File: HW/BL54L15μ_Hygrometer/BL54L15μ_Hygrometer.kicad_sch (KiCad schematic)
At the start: 36 parts, among them IC1 nrf54L 453-00223R, J1 Conn_Qwiic, J2 Conn_ARM_JTAG_SWD_10, SW1 Reset, U1 nPM2100-QEXX, U2 SHT4x, U3 STCC4-D-R3, U5 BME688, X1 32.768 kHz

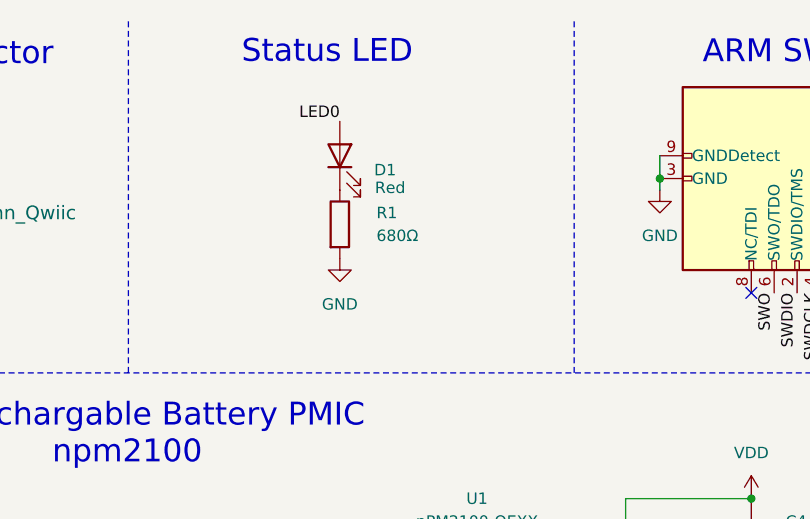
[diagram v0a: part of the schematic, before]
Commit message: Cleanup Hygrometer BOM
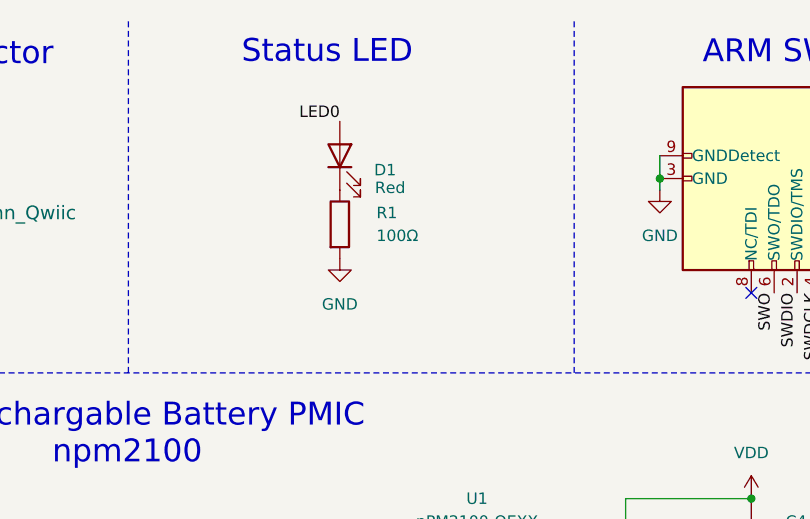
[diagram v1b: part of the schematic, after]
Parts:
- R1: value 680Ω -> 100Ω; Part Number RC0603JR-13680RL -> RC0603FR-07100RL
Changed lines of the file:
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@@
 			)
 		)
-		(property "Value" "680Ω"
+		(property "Value" "100Ω"
 			(at 87.884 36.83 0)
 			(effects
@@
 			)
 		)
-		(property "Part Number" "RC0603JR-13680RL"
+		(property "Part Number" "RC0603FR-07100RL"
 			(at 83.82 35.56 0)
 			(effects

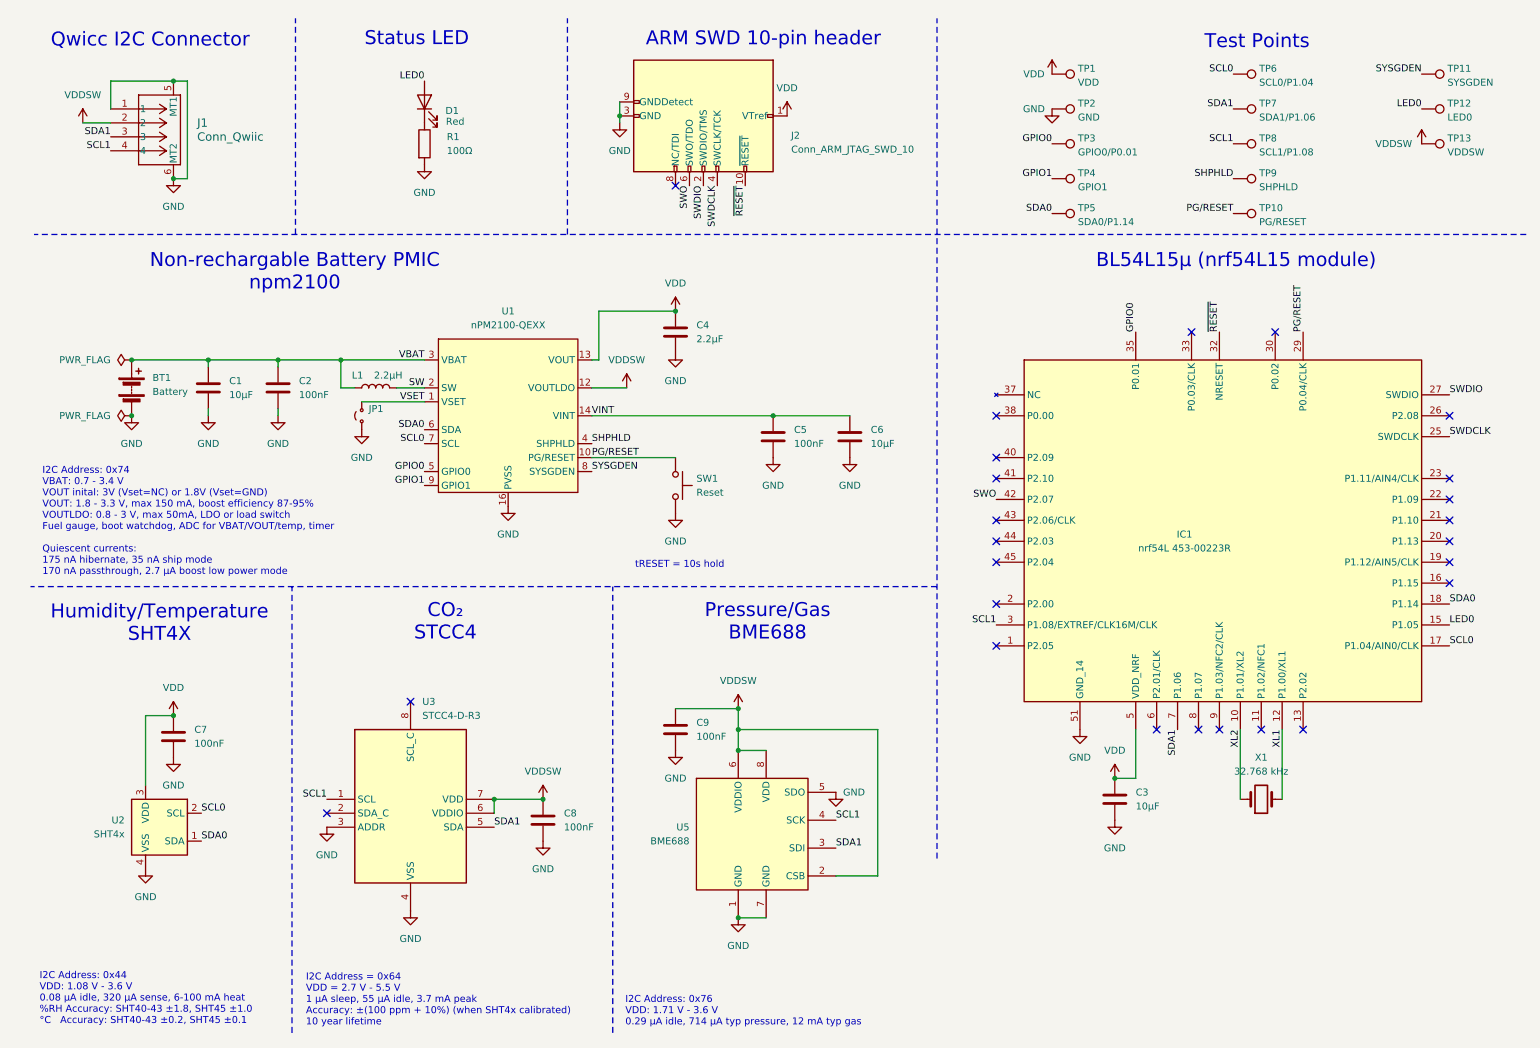
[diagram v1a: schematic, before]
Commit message: BL54L15μ Hygrometer 2026v4 with leak sensing
- Switch to CR2 battery
- Drop power-hungry STCC4/BME688 sensors
- Circular design with M1.2 mounting holes
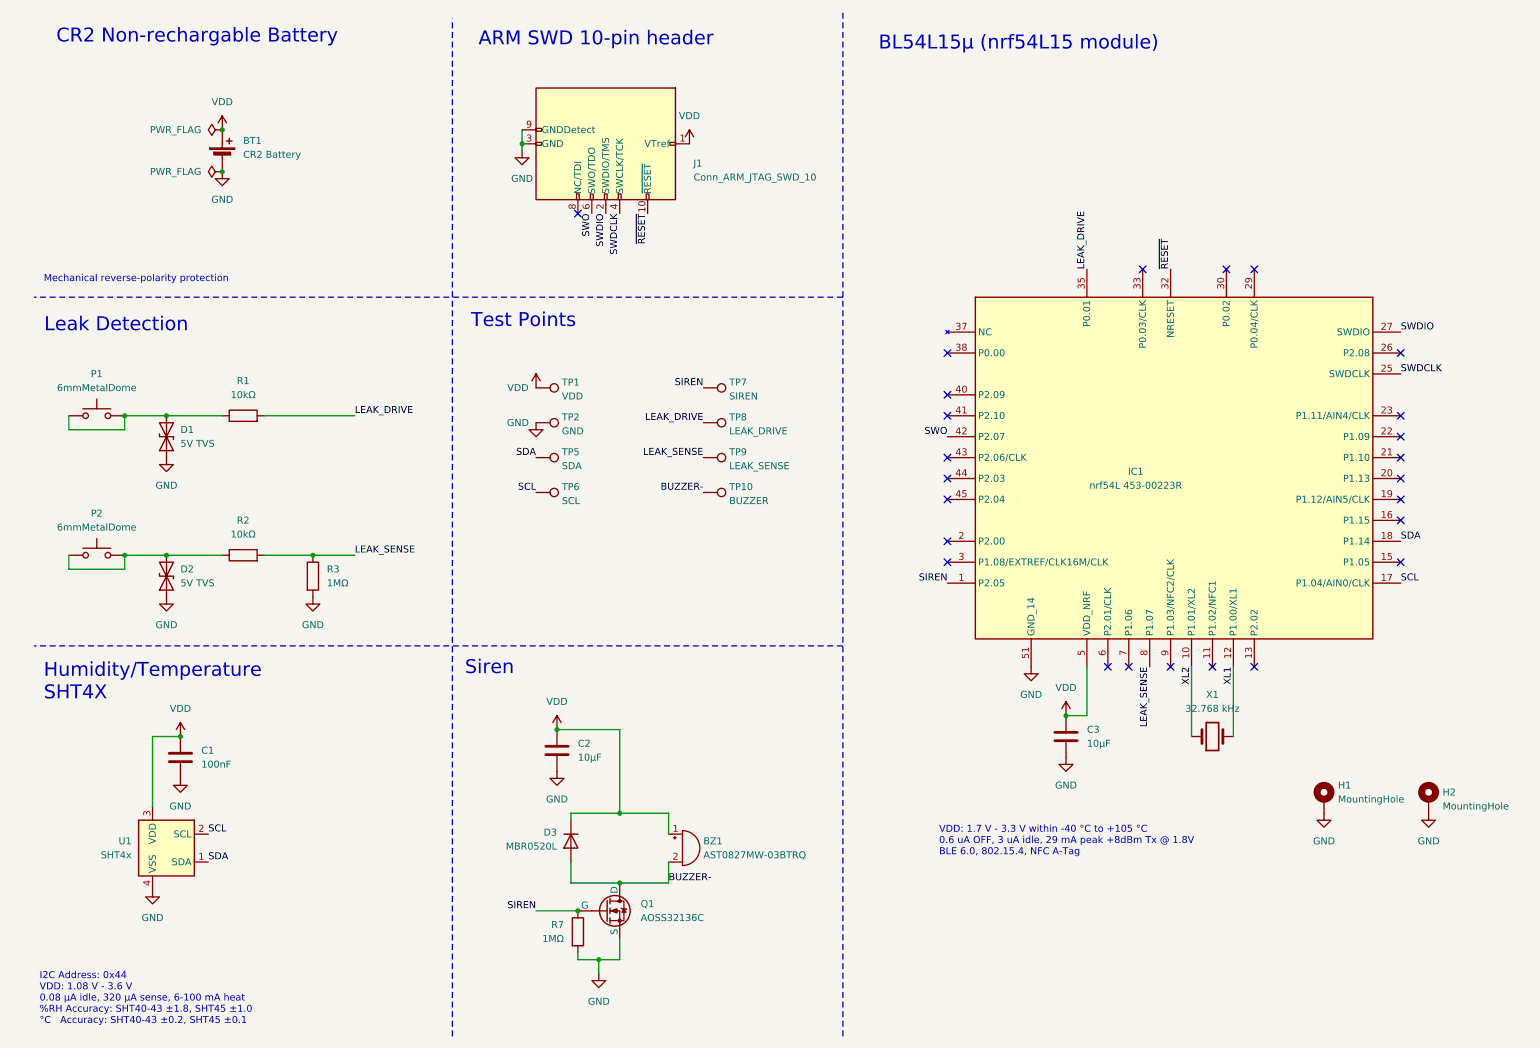
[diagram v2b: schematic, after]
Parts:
- removed C1, C6: 10μF, Capacitor_SMD:C_0603_1608Metric, symbol Device:C
- removed C4: 2.2μF, Capacitor_SMD:C_0402_1005Metric, symbol Device:C
- removed C5, C8, C9: 100nF, Capacitor_SMD:C_0402_1005Metric, symbol Device:C
- removed D1: PWRLED, LED_SMD:LED_0603_1608Metric, symbol Device:LED
- removed J1: Conn_Qwiic, SM04B_SRSS_TB:CONN_SM04B-SRSS-TB_JST, symbol SM04B_SRSS_TB:SM04B-SRSS-TB
- removed JP1: VSET-GND, Jumper:SolderJumper-2_P1.3mm_Open_RoundedPad1.0x1.5mm, symbol Jumper:Jumper_2_Small_Open
- removed L1: 2.2μH, CIGT201610EH2R2MNE:IND_CIGT2016_SAM, symbol Device:L
- removed SW1: Reset, Button_Switch_SMD:SW_Push_SPST_NO_Alps_SKRK, symbol Switch:SW_Push
- removed TP11: SYSGDEN, TestPoint:TestPoint_Pad_D1.0mm, symbol Connector:TestPoint
- removed TP12: LED0, TestPoint:TestPoint_Pad_D1.0mm, symbol Connector:TestPoint
- removed TP13: VDDSW, TestPoint:TestPoint_Pad_D1.0mm, symbol Connector:TestPoint
- removed TP3: GPIO0/P0.01, TestPoint:TestPoint_Pad_D1.0mm, symbol Connector:TestPoint
- removed TP4: GPIO1, TestPoint:TestPoint_Pad_D1.0mm, symbol Connector:TestPoint
- removed U1: nPM2100-QEXX, Package_DFN_QFN:UQFN-16-1EP_4x4mm_P0.65mm_EP2.6x2.6mm, symbol Nordic_nPM:nPM2100-QEXX
- removed U3: STCC4-D-R3, STCC4-D-R3:STCC4DR3, symbol STCC4-D-R3:STCC4-D-R3
- removed U5: BME688, Package_LGA:Bosch_LGA-8_3x3mm_P0.8mm_ClockwisePinNumbering, symbol BME680:BME680
- added BZ1: AST0827MW-03BTRQ, AST0827MW-03BTRQ:AST0827MW-03BTRQ_MAL, symbol Device:Buzzer
- added D1, D2: 5V TVS, Diode_SMD:D_0402_1005Metric, symbol Device:D_TVS
- added D3: MBR0520L, Diode_SMD:D_SOD-123, symbol Device:D
- added H1, H2: MountingHole, MountingHoleCompact:MountingHole_M1.2_1.3mm_Plated, symbol Mechanical:MountingHole_Pad
- added P1, P2: 6mmMetalDome, MetalDomeSwitch:TriangleDome_Diameter6mm, symbol Switch:SW_Push
- added Q1: AOSS32136C, Package_TO_SOT_SMD:SOT-23-3, symbol Simulation_SPICE:NMOS
- added R2: 10kΩ, Resistor_SMD:R_0402_1005Metric, symbol Device:R
- added R3, R7: 1MΩ, Resistor_SMD:R_0402_1005Metric, symbol Device:R
- BT1: value Battery -> CR2 Battery; footprint BatteryHolder_Keystone_2468_2xAAA_NoHoles:BatteryHolder_Keystone_2468_2xAAA -> 1011:BAT_1011; symbol Device:Battery -> Device:Battery_Cell; Digikey Part Number 36-2468-ND -> (none); Manufacturer (none) -> Keystone Electronics; Part Number (none) -> 1011
- C1: renamed from C7; Manufacturer (none) -> Murata Electronics
- C2: value 100nF -> 10μF; footprint Capacitor_SMD:C_0402_1005Metric -> Capacitor_SMD:C_0603_1608Metric; Manufacturer (none) -> Samsung Electro-Mechanics; Part Number GRM155R61A104KA01J -> CL10A106KP8NNNC
- C3: Manufacturer (none) -> Samsung Electro-Mechanics
- IC1: Manufacturer (none) -> EZURIO; Manufacturer_Name EZURIO -> (none)
- J1: renamed from J2; Digikey Part Number 1528-752-ND -> (none); Manufacturer (none) -> CNC Tech; Part Number (none) -> 3220-10-0300-00
- R1: value 100Ω -> 10kΩ; footprint Resistor_SMD:R_0603_1608Metric -> Resistor_SMD:R_0402_1005Metric; Manufacturer (none) -> YAGEO; Part Number RC0603FR-07100RL -> RC0402FR-0710KL
- TP10: value PG/RESET -> BUZZER
- TP5: value SDA0/P1.14 -> SDA
- TP6: value SCL0/P1.04 -> SCL
- TP7: value SDA1/P1.06 -> SIREN
- TP8: value SCL1/P1.08 -> LEAK_DRIVE
- TP9: value SHPHLD -> LEAK_SENSE
- U1: renamed from U2; Manufacturer (none) -> Sensirion AG
- X1: Manufacturer (none) -> Micro Crystal AG
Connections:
- net SHPHLD is gone; now on net LEAK_SENSE: TP9.1
- net VBAT is gone; now on net VDD: BT1.1 (+), C2.1
- net GND: now also D1.1 (A1), D2.1 (A1), H1.1, H2.1, Q1.3 (S), R3.2, R7.2; no longer R1.2
- net VDD: now also BZ1.1 (+), D3.1 (K)
- net at R1.1: now also D1.2 (A2), P1.1, P1.2
- net SIREN: now reaches IC1.1 (P2.05)
- net SIREN: now also TP7.1, Q1.2 (G), R7.1
- net LEAK_SENSE: now reaches IC1.8 (P1.07)
- net LEAK_SENSE: now also R2.2, R3.1
- net GPIO0 renamed LEAK_DRIVE
- net LEAK_DRIVE: now also R1.2, TP8.1
- net LED0: no longer names the net of IC1.15 (P1.05)
- net PG/RESET: no longer names the net of IC1.29 (P0.04/CLK)
- net PG/RESET: no longer TP10.1
- net SCL0 renamed SCL
- net SCL1: no longer names the net of IC1.3 (P1.08/EXTREF/CLK16M/CLK)
- net SCL1: no longer TP8.1
- net SDA0 renamed SDA
- net SDA1: no longer names the net of IC1.7 (P1.06)
- net SDA1: no longer TP7.1
- new net: D2.2 (A2), P2.1, P2.2, R2.1
- new net BUZZER-: BZ1.2 (-), D3.2 (A), Q1.1 (D), TP10.1
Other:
- note added: "CR2 Non-rechargable Battery"
- note added: "Leak Detection"
- note added: "Mechanical reverse-polarity protection"
- note added: "Siren"
- note added: "VDD: 1.7 V - 3.3 V within -40 °C to +105 °C 0.6 uA OFF, 3 uA idle, 29 mA peak +8dBm Tx @ 1.8V BLE 6.0, 802.15.4, NFC A-Tag"
- note removed: "CO₂ STCC4"
- note removed: "I2C Address = 0x64 VDD = 2.7 V - 5.5 V 1 μA sleep, 55 μA idle, 3.7 mA peak Accuracy: ±(100 ppm + 10%) (when SHT4x calibrated) 10 year lifetime"
- note removed: "I2C Address: 0x74 VBAT: 0.7 - 3.4 V VOUT inital: 3V (Vset=NC) or 1.8V (Vset=GND) VOUT: 1.8 - 3.3 V, max 150 mA, boost efficiency 87-95% VOUTLDO: 0.8 - 3 V, max 50mA, LDO or load switch Fuel gauge, boot watchdog, ADC for VBAT/VOUT/temp, timer Quiescent currents: 175 nA hibernate, 35 nA ship mode 170 nA passthrough, 2.7 µA boost low power mode"
- note removed: "I2C Address: 0x76 VDD: 1.71 V - 3.6 V 0.29 μA idle, 714 μA typ pressure, 12 mA typ gas"
- note removed: "Non-rechargable Battery PMIC npm2100"
- note removed: "Pressure/Gas BME688"
- note removed: "Qwicc I2C Connector"
- note removed: "Status LED"
- note removed: "tRESET = 10s hold"
- moved on the sheet: C1, C3, IC1, J1, TP1, TP2, TP5, TP6, U1, X1
